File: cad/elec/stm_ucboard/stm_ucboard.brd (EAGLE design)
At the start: 34 x 14 mm, 21 parts

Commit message: small fixes to stm uc board
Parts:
- removed C3: 4u7, rcl:C0603
- added C2: 100n, rcl:C0603
- moved C1 1.52 mm to (13.6, 2.44)
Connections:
- net +3V3: now also C2.2; no longer C3.2
- net GND: now also C2.1; no longer C3.1
- net LED_R: now also U$1.17; no longer U$1.15
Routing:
- net LED_G: track 15.9 -> 12.3 mm
- net GND: track 42.6 -> 39.6 mm
- net LED_R: track 15.6 -> 13.5 mm
- net +3V3: track 58.3 -> 60.2 mm

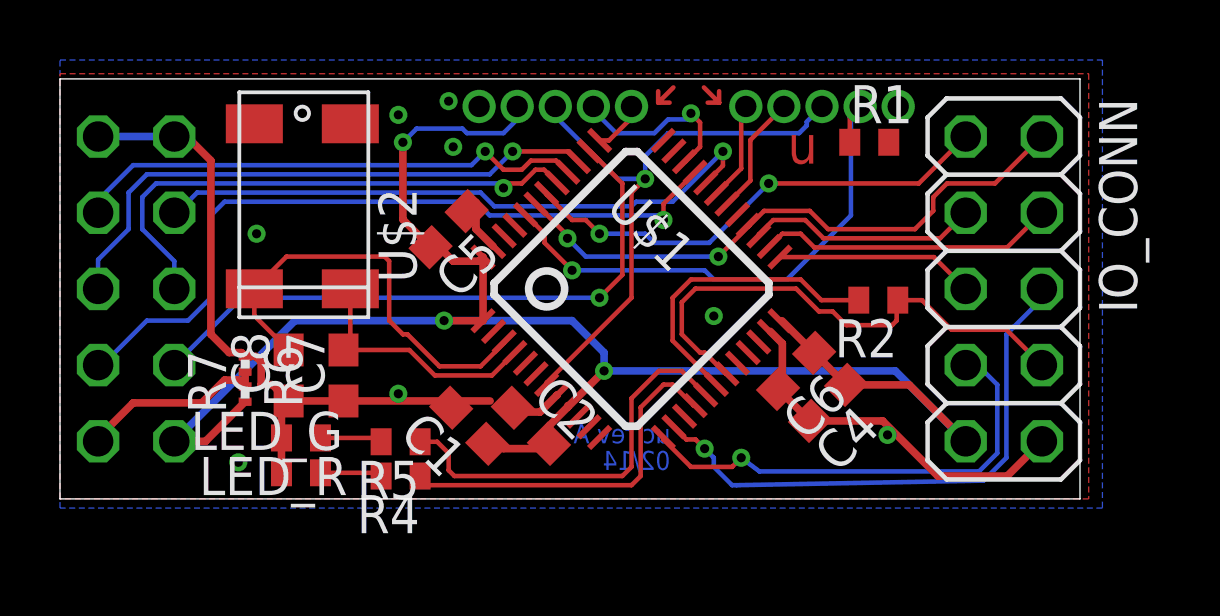
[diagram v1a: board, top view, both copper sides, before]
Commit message: made drills of debug connectors smaller
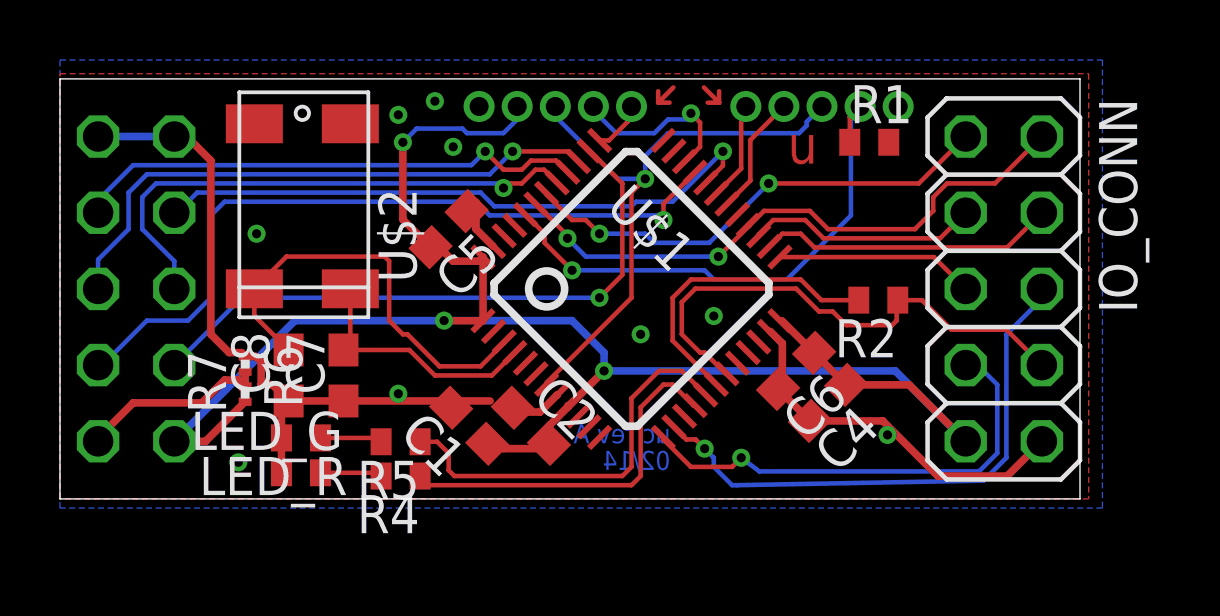
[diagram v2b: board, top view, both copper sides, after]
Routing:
- net GND: vias 8 -> 9
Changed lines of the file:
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@@
 <vertex x="0" y="-0.3048"/>
 </polygon>
-<via x="12.954" y="13.2588" extent="1-16" drill="0.3048"/>
+<via x="12.4968" y="13.2588" extent="1-16" drill="0.3048"/>
 <via x="13.1064" y="11.7348" extent="1-16" drill="0.3048"/>
 <via x="11.2776" y="12.8016" extent="1-16" drill="0.3048"/>
@@
 <wire x1="16.002" y1="2.8956" x2="15.239996875" y2="2.8956" width="0.254" layer="1"/>
 <wire x1="15.239996875" y1="2.8956" x2="15.09615625" y2="3.039440625" width="0.254" layer="1"/>
+<via x="19.3548" y="5.4864" extent="1-16" drill="0.3048"/>
 </signal>
 <signal name="+3V3">
